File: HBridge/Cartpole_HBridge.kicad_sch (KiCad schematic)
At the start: 13 parts, among them J1 Conn_01x12_Pin, J2 Barrel_Jack, J3 Conn_01x06_Socket, Q1 BSS84P, U1 TB6612FNG

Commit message: Upped the footprint size of the 470uf cap
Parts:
- C4: footprint Capacitor_SMD:C_1206_3216Metric_Pad1.33x1.80mm_HandSolder -> Capacitor_SMD:C_1812_4532Metric_Pad1.57x3.40mm_HandSolder
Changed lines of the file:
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@@
 			)
 		)
-		(property "Footprint" "Capacitor_SMD:C_1206_3216Metric_Pad1.33x1.80mm_HandSolder"
+		(property "Footprint" "Capacitor_SMD:C_1812_4532Metric_Pad1.57x3.40mm_HandSolder"
 			(at 36.83 44.1452 0)
 			(effects

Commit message: Changed 470uf cap to one more readily availible
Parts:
- removed C4: 470, Capacitor_SMD:C_1812_4532Metric_Pad1.57x3.40mm_HandSolder, symbol Device:C
- added C4: 470, Capacitor_SMD:C_Elec_6.3x7.7, symbol Device:C_Polarized_US
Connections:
- net GND: now also C4.2
- net at J2.1, Q1.3 (D): now also C4.1
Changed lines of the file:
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@@
+	)
+	(symbol
+		(lib_id "Device:C_Polarized_US")
+		(at 40.64 43.18 270)
+		(unit 1)
+		(exclude_from_sim no)
+		(in_bom yes)
+		(on_board yes)
+		(dnp no)
+		(fields_autoplaced yes)
+		(property "Reference" "C4"
+			(at 41.275 35.56 90)
+			(effects
+				(font
+					(size 1.27 1.27)
+				)
+			)
+		)
+		(property "Value" "470"
+			(at 41.275 38.1 90)
+			(effects
+				(font
+					(size 1.27 1.27)
+				)
+			)
+		)
+		(property "Footprint" "Capacitor_SMD:C_Elec_6.3x7.7"
+			(at 40.64 43.18 0)
+			(effects
+				(font
+					(size 1.27 1.27)
+				)
+				(hide yes)
+			)
+		)
+		(property "Datasheet" "~"
+			(at 40.64 43.18 0)
+			(effects
+				(font
+					(size 1.27 1.27)
+				)
+				(hide yes)
+			)
+		)
+		(property "Description" "Polarized capacitor, US symbol"
+			(at 40.64 43.18 0)
+			(effects
+				(font
+					(size 1.27 1.27)
+				)
+				(hide yes)
+			)
+		)
+		(pin "1"
+		)
+		(pin "2"
+		)
+		(instances
+			(project ""
+				(path "/60393b33-8cba-40b2-8444-0a09a94036dc"
+					(reference "C4")
+					(unit 1)
+				)
+			)
+		)
 	)
 	(symbol
@@
 					(unit 1)
 				)
-			)
-		)
-	)
-	(symbol
-		(lib_id "Device:C")
-		(at 40.64 43.18 270)
-		(unit 1)
-		(exclude_from_sim no)
-		(in_bom yes)
-		(on_board yes)
-		(dnp no)
-		(fields_autoplaced yes)
-		(property "Reference" "C4"
-			(at 40.64 35.56 90)
-			(effects
-				(font
-					(size 1.27 1.27)
-				)
-			)
-		)
-		(property "Value" "470"
-			(at 40.64 38.1 90)
-			(effects
-				(font
-					(size 1.27 1.27)
-				)
-			)
-		)
-		(property "Footprint" "Capacitor_SMD:C_1812_4532Metric_Pad1.57x3.40mm_HandSolder"
-			(at 36.83 44.1452 0)
-			(effects
-				(font
-					(size 1.27 1.27)
-				)
-				(hide yes)
-			)
-		)
-		(property "Datasheet" "~"
-			(at 40.64 43.18 0)
-			(effects
-				(font
-					(size 1.27 1.27)
-				)
-				(hide yes)
-			)
-		)
-		(property "Description" "Unpolarized capacitor"
-			(at 40.64 43.18 0)
-			(effects
-				(font
-					(size 1.27 1.27)
-				)
-				(hide yes)
-			)
-		)
-		(pin "1"
-		)
-		(pin "2"
-		)
-		(instances
-			(project ""
-				(path "/60393b33-8cba-40b2-8444-0a09a94036dc"
-					(reference "C4")
-					(unit 1)
-				)

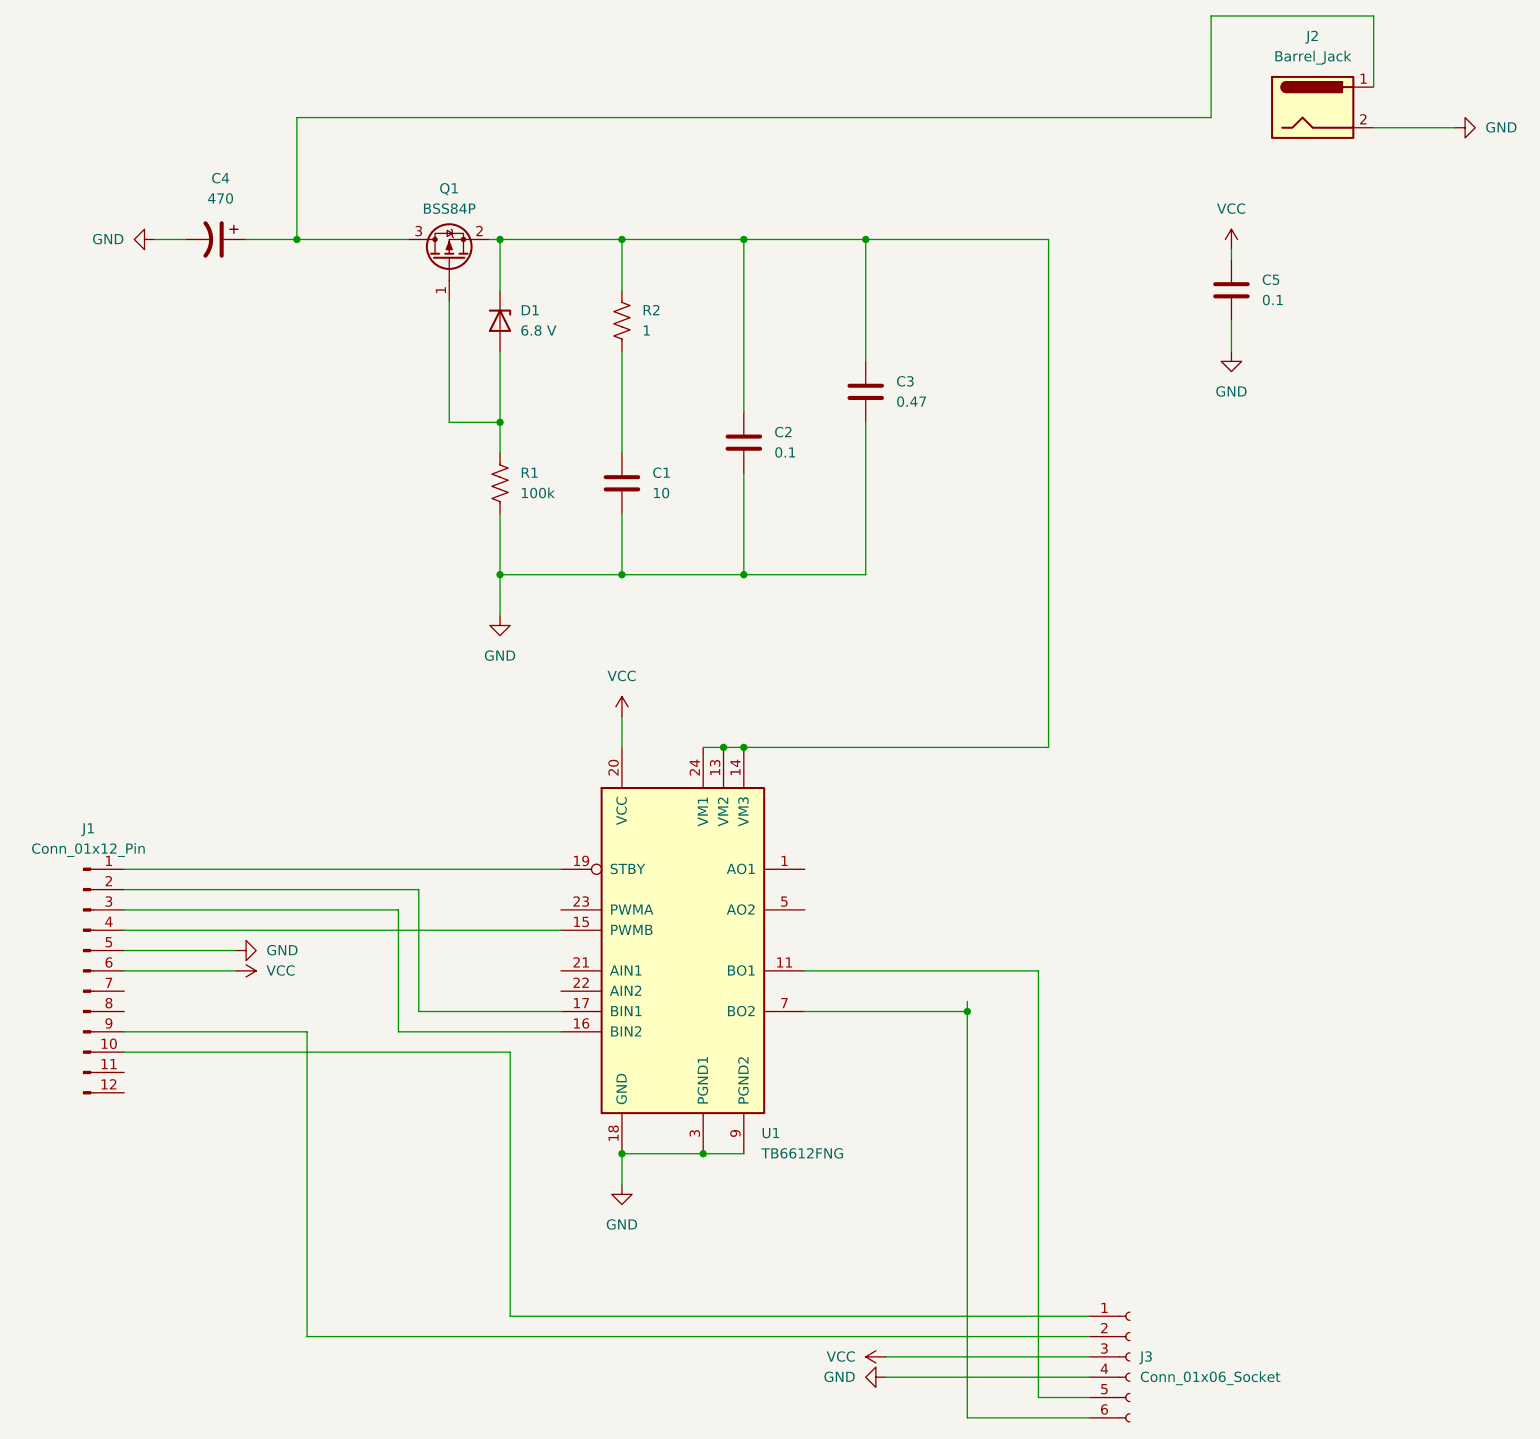
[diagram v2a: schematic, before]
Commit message: Compressed size of board to be within PMod spec
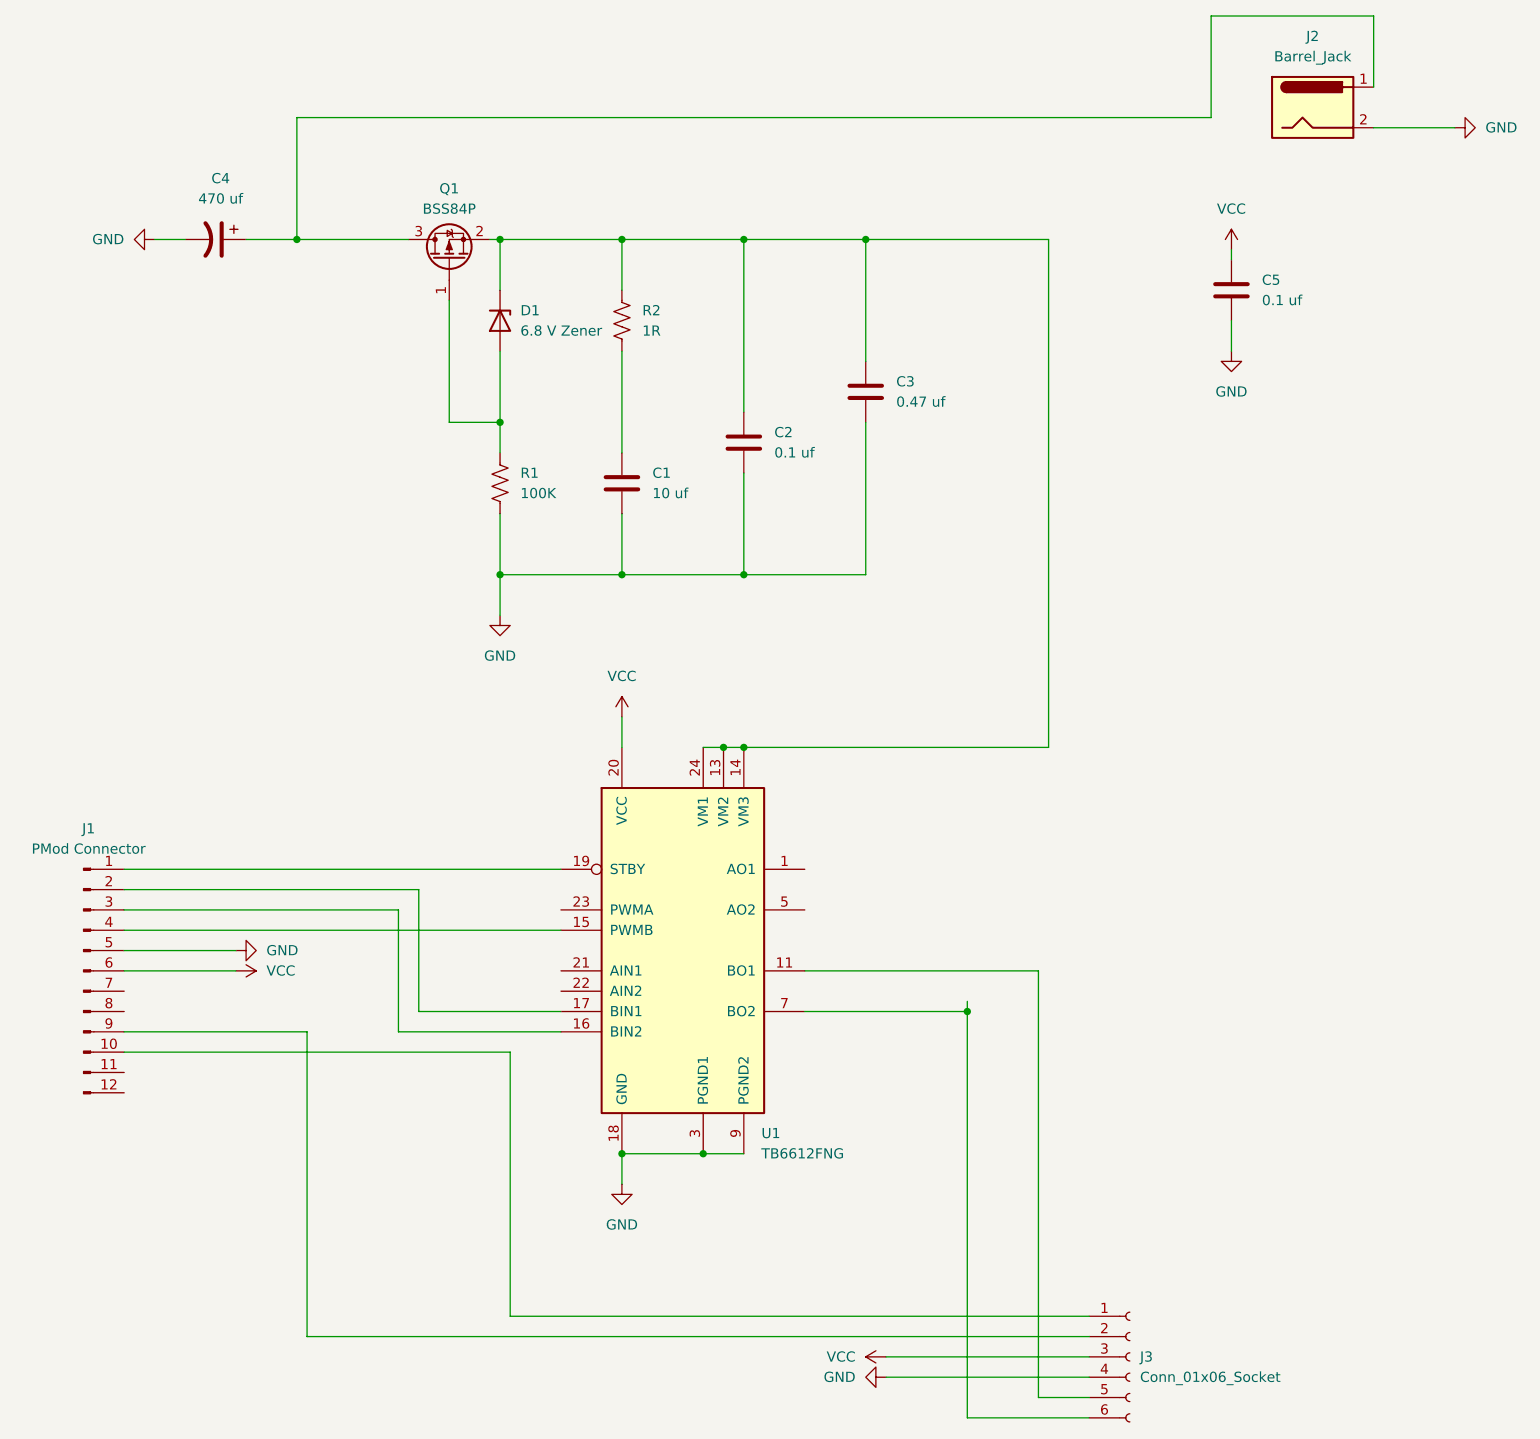
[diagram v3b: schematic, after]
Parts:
- C1: value 10 -> 10 uf
- C2, C5: value 0.1 -> 0.1 uf
- C3: value 0.47 -> 0.47 uf
- C4: value 470 -> 470 uf
- D1: value 6.8 V -> 6.8 V Zener
- J1: value Conn_01x12_Pin -> PMod Connector
- R1: value 100k -> 100K
- R2: value 1 -> 1R
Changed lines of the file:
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@@
 			)
 		)
-		(property "Value" "10"
+		(property "Value" "10 uf"
 			(at 95.25 74.9299 0)
 			(effects
@@
 			)
 		)
-		(property "Value" "470"
+		(property "Value" "470 uf"
 			(at 41.275 38.1 90)
 			(effects
@@
 			)
 		)
-		(property "Value" "0.1"
+		(property "Value" "0.1 uf"
 			(at 171.45 50.7999 0)
 			(effects
@@
 			)
 		)
-		(property "Value" "100k"
+		(property "Value" "100K"
 			(at 78.74 74.9299 0)
 			(effects
@@
 			)
 		)
-		(property "Value" "0.47"
+		(property "Value" "0.47 uf"
 			(at 125.73 63.4999 0)
 			(effects
@@
 			)
 		)
-		(property "Value" "0.1"
+		(property "Value" "0.1 uf"
 			(at 110.49 69.8499 0)
 			(effects
@@
 			)
 		)
-		(property "Value" "Conn_01x12_Pin"
+		(property "Value" "PMod Connector"
 			(at 24.765 119.38 0)
 			(effects
@@
 			)
 		)
-		(property "Value" "6.8 V"
+		(property "Value" "6.8 V Zener"
 			(at 78.74 54.6099 90)
 			(effects
@@
 			)
 		)
-		(property "Datasheet" "http://www.farnell.com/datasheets/1835997.pdf"
+		(property "Datasheet" "https://www.diodes.com/assets/Datasheets/BSS84.pdf"
 			(at 73.66 40.64 0)
 			(effects
@@
 			)
 		)
-		(property "Value" "1"
+		(property "Value" "1R"
 			(at 93.98 54.6099 0)
 			(effects
